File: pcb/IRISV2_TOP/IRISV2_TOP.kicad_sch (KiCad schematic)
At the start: 18 parts, among them J1 Conn_01x20_MountingPin, J2 USB_C_Receptacle_USB2.0_16P, J3 USB_C_Receptacle_USB2.0_16P, J9 Conn_01x06_MountingPin

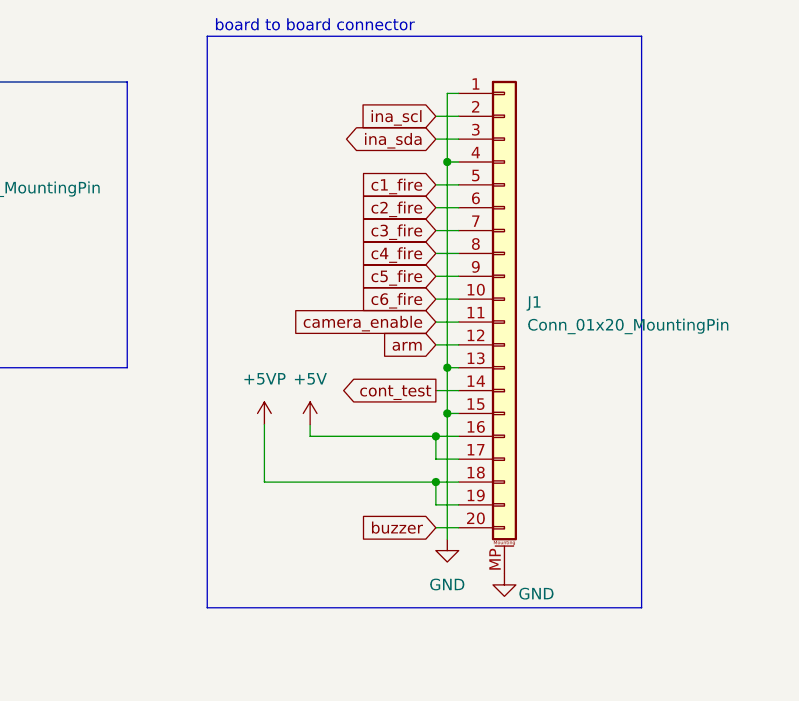
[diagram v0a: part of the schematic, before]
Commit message: all main routing done, need to break out remaining gpio onto banks of mpu and ppu
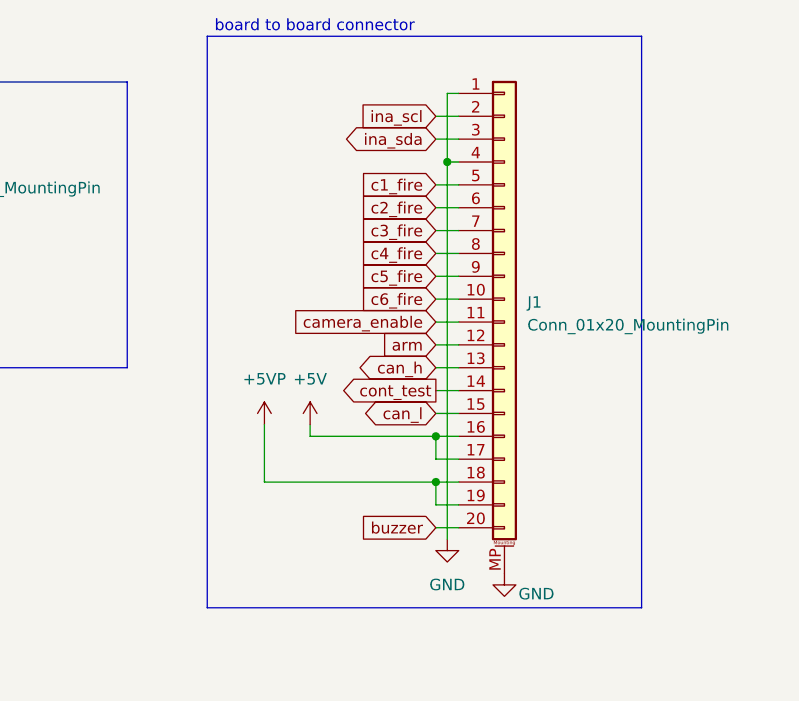
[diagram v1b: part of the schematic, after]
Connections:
- net GND: no longer J1.13 (Pin_13), J1.15 (Pin_15)
- new net can_h: J1.13 (Pin_13)
- new net can_l: J1.15 (Pin_15)
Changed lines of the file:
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@@
-	)
-	(junction
-		(at 245.11 128.27)
-		(diameter 0)
-		(color 0 0 0 0)
 	)
 	(junction
@@
 	)
 	(junction
-		(at 245.11 123.19)
-		(diameter 0)
-		(color 0 0 0 0)
-	)
-	(junction
 		(at 49.53 137.16)
 		(diameter 0)
@@
 	(wire
 		(pts
-			(xy 245.11 128.27) (xy 246.38 128.27)
-		)
-		(stroke
-			(width 0)
-			(type default)
-		)
-	)
-	(wire
-		(pts
 			(xy 243.84 118.11) (xy 246.38 118.11)
 		)
@@
 	(wire
 		(pts
-			(xy 245.11 128.27) (xy 245.11 142.24)
+			(xy 243.84 123.19) (xy 246.38 123.19)
 		)
 		(stroke
@@
 	(wire
 		(pts
-			(xy 245.11 123.19) (xy 246.38 123.19)
-		)
-		(stroke
-			(width 0)
-			(type default)
-		)
-	)
-	(wire
-		(pts
 			(xy 58.42 129.54) (xy 57.15 129.54)
 		)
@@
 	(wire
 		(pts
+			(xy 243.84 128.27) (xy 246.38 128.27)
+		)
+		(stroke
+			(width 0)
+			(type default)
+		)
+	)
+	(wire
+		(pts
+			(xy 245.11 100.33) (xy 245.11 142.24)
+		)
+		(stroke
+			(width 0)
+			(type default)
+		)
+	)
+	(wire
+		(pts
 			(xy 49.53 142.24) (xy 48.26 142.24)
 		)
@@
 		(pts
 			(xy 243.84 120.65) (xy 246.38 120.65)
-		)
-		(stroke
-			(width 0)
-			(type default)
-		)
-	)
-	(wire
-		(pts
-			(xy 245.11 123.19) (xy 245.11 128.27)
-		)
-		(stroke
-			(width 0)
-			(type default)
-		)
-	)
-	(wire
-		(pts
-			(xy 245.11 100.33) (xy 245.11 123.19)
 		)
 		(stroke
@@
 		)
 	)
+	(global_label "can_l"
+		(shape bidirectional)
+		(at 243.84 128.27 180)
+		(fields_autoplaced yes)
+		(effects
+			(font
+				(size 1.27 1.27)
+			)
+			(justify right)
+		)
+		(property "Intersheetrefs" "${INTERSHEET_REFS}"
+			(at 234.7241 128.27 0)
+			(effects
+				(font
+					(size 1.27 1.27)
+				)
+				(justify right)
+				(hide yes)
+			)
+		)
+	)
 	(global_label "gps_mtx"
 		(shape input)
@@
 			(effects
 				(font
+					(size 1.27 1.27)
+				)
+				(justify right)
+				(hide yes)
+			)
+		)
+	)
+	(global_label "can_h"
+		(shape bidirectional)
+		(at 243.84 123.19 180)
+		(fields_autoplaced yes)
+		(effects
+			(font
+				(size 1.27 1.27)
+			)
+			(justify right)
+		)
+		(property "Intersheetrefs" "${INTERSHEET_REFS}"
+			(at 234.2403 123.19 0)
+			(effects
+				(font

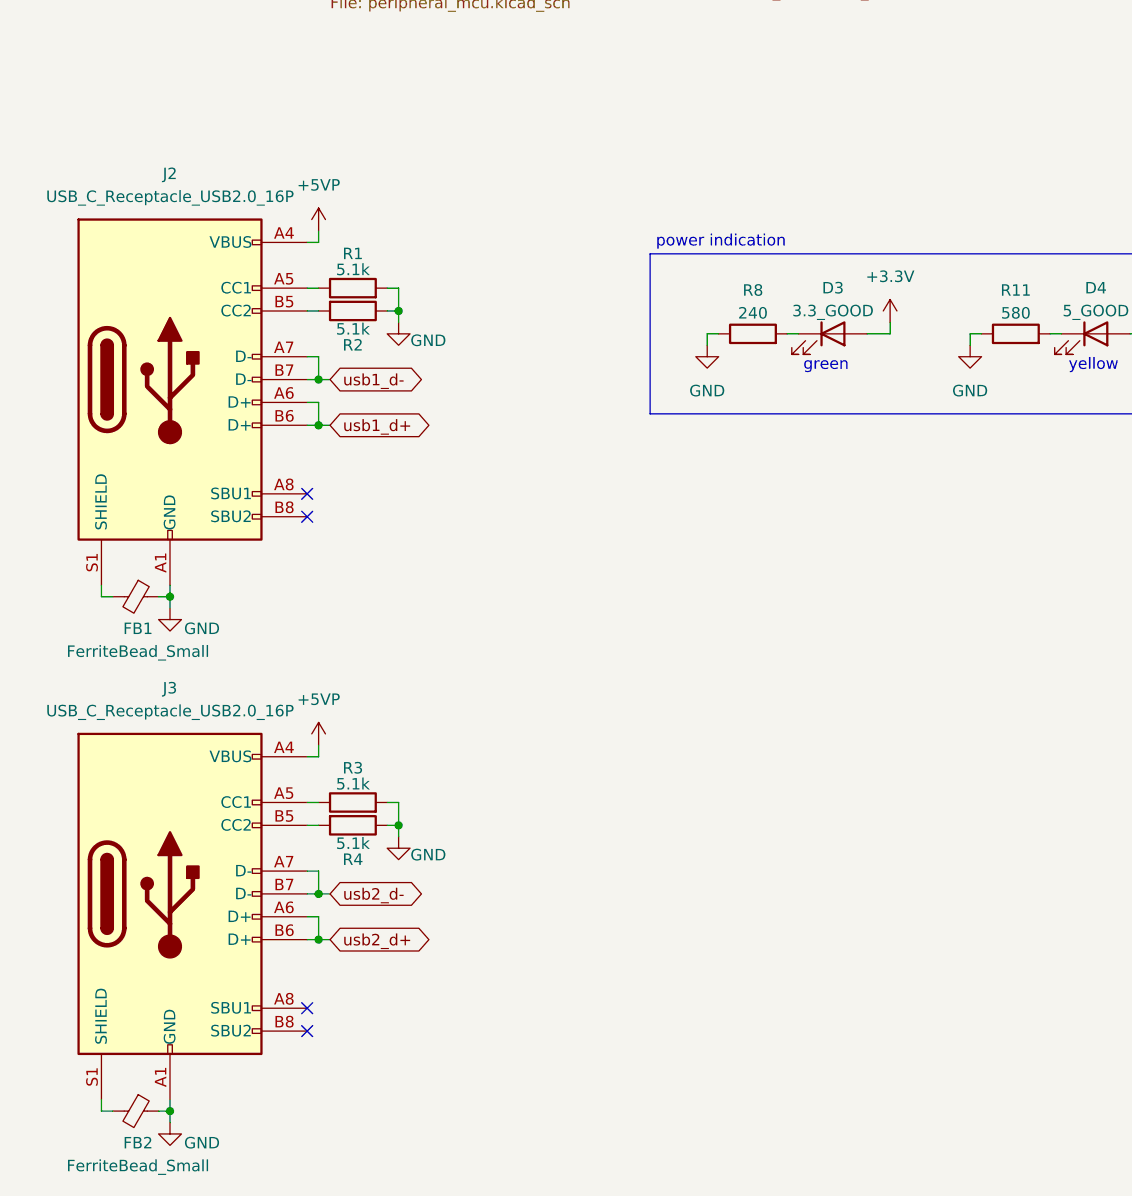
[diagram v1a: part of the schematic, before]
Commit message: removed usb, added connectors and stuff, 3d models mostly added, still need to route out gpio and servos (though connectors added)
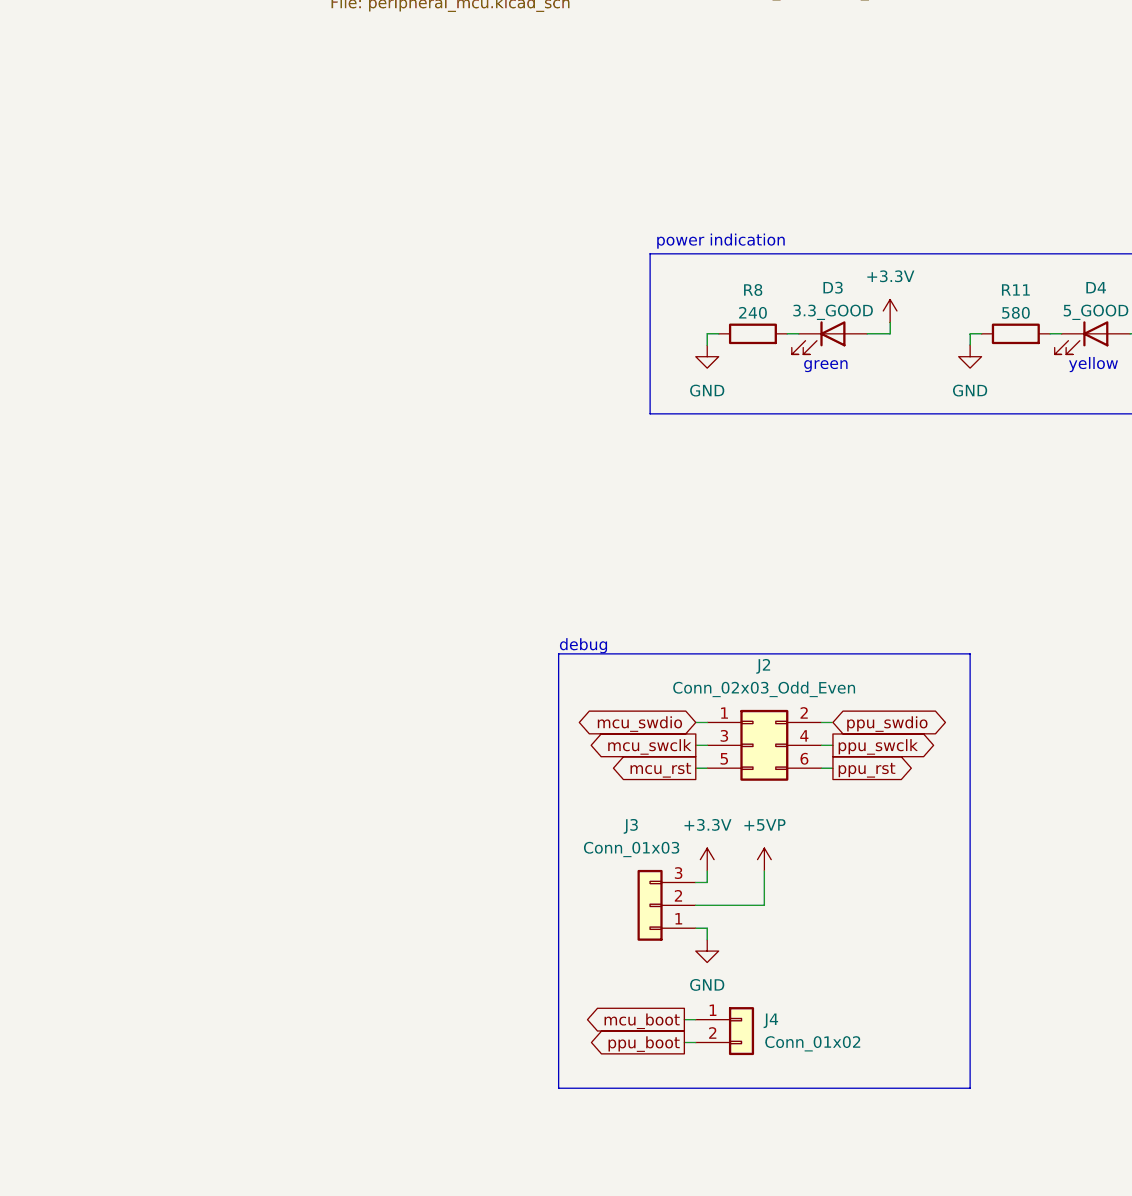
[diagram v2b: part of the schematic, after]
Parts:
- removed FB1, FB2: FerriteBead_Small, Inductor_SMD:L_0402_1005Metric, symbol Device:FerriteBead_Small
- removed J2, J3: USB_C_Receptacle_USB2.0_16P, UJ20-C-H-G-SMT-1-P16-TR:SAMESKY_UJ20-C-H-G-SMT-1-P16-TR, symbol Connector:USB_C_Receptacle_USB2.0_16P
- removed R1, R2, R3, R4: 5.1k, Resistor_SMD:R_0402_1005Metric, symbol Device:R
- added J2: Conn_02x03_Odd_Even, Connector_PinHeader_2.54mm:PinHeader_2x03_P2.54mm_Vertical, symbol Connector_Generic:Conn_02x03_Odd_Even
- added J3: Conn_01x03, Connector_PinHeader_2.54mm:PinHeader_1x03_P2.54mm_Vertical, symbol Connector_Generic:Conn_01x03
- added J4: Conn_01x02, Connector_PinHeader_2.54mm:PinHeader_1x02_P2.54mm_Vertical, symbol Connector_Generic:Conn_01x02
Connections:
- net +3.3V: now also J3.3 (Pin_3)
- net +5VP: now also J3.2 (Pin_2)
- net GND: now also J3.1 (Pin_1)
- new net mcu_boot: J4.1 (Pin_1)
- new net mcu_rst: J2.5 (Pin_5)
- new net mcu_swclk: J2.3 (Pin_3)
- new net mcu_swdio: J2.1 (Pin_1)
- new net ppu_boot: J4.2 (Pin_2)
- new net ppu_rst: J2.6 (Pin_6)
- new net ppu_swclk: J2.4 (Pin_4)
- new net ppu_swdio: J2.2 (Pin_2)
- no-connect marks 4 -> 0
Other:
- note added: "debug"

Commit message: pcb hopefully mostly finalized
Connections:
- net GND: no longer J1.1 (Pin_1), J1.4 (Pin_4)
- new net cam_uart_rx: J1.4 (Pin_4)
- new net cam_uart_tx: J1.1 (Pin_1)
